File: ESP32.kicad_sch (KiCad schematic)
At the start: 6 parts, among them J9 PROG, U4 ESP32-WROOM-32D

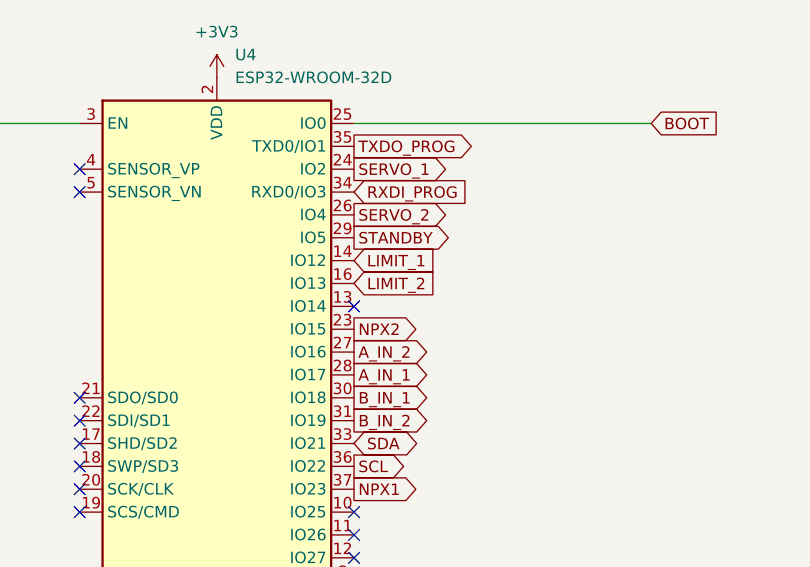
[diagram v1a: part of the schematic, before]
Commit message: Moved LIMIT1 signal away from IO12 where the pullup was stopping the ESP from booting
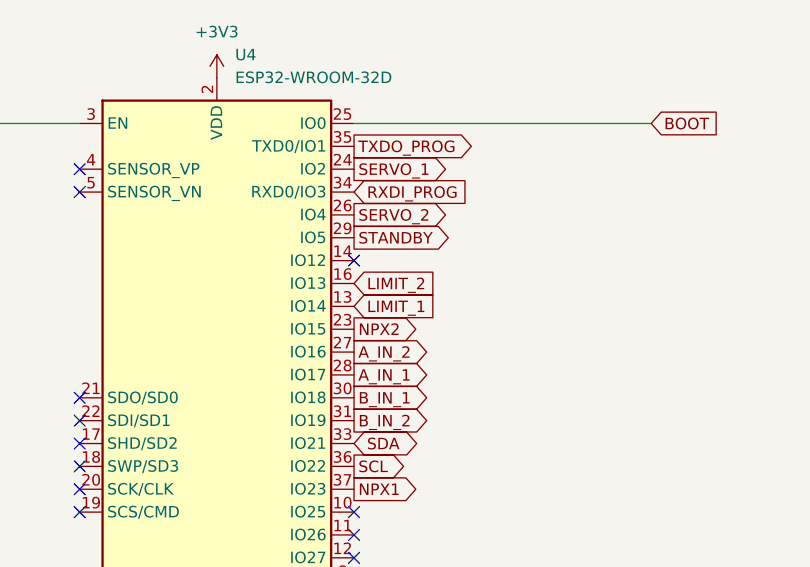
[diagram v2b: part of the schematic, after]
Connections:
- net LIMIT_1: now also U4.13 (IO14); no longer U4.14 (IO12)
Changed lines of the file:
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@@
   )
   (no_connect (at 223.52 106.68))
+  (no_connect (at 223.52 78.74))
   (no_connect (at 223.52 109.22))
   (no_connect (at 193.04 104.14))
@@
   (no_connect (at 193.04 68.58))
   (no_connect (at 193.04 71.12))
-  (no_connect (at 223.52 83.82))
   (no_connect (at 223.52 111.76))
   (polyline (pts (xy 124.46 24.13) (xy 124.46 161.29))
@@
     )
   )
-  (global_label "LIMIT_1" (shape input) (at 223.52 78.74 0) (fields_autoplaced)
-    (effects (font (size 1.27 1.27)) (justify left))
-    (property "Intersheet References" "${INTERSHEET_REFS}" (id 0) (at 232.7669 78.6606 0)
+  (global_label "LIMIT_1" (shape input) (at 223.52 83.82 0) (fields_autoplaced)
+    (effects (font (size 1.27 1.27)) (justify left))
+    (property "Intersheet References" "${INTERSHEET_REFS}" (id 0) (at 232.7669 83.7406 0)
       (effects (font (size 1.27 1.27)) (justify left) hide)
     )
@@
     (pin "6")
   )
-  (symbol (lib_name "+3V3_2") (lib_id "power:+3V3") (at 67.31 43.18 0) (unit 1)
+  (symbol (lib_id "power:+3V3") (at 67.31 43.18 0) (unit 1)
     (in_bom yes) (on_board yes) (fields_autoplaced)
     (property "Reference" "#PWR029" (id 0) (at 67.31 46.99 0)
@@
     (pin "1")
   )
-  (symbol (lib_name "+3V3_3") (lib_id "power:+3V3") (at 173.99 55.88 0) (unit 1)
+  (symbol (lib_id "power:+3V3") (at 173.99 55.88 0) (unit 1)
     (in_bom yes) (on_board yes) (fields_autoplaced)
     (property "Reference" "#PWR030" (id 0) (at 173.99 59.69 0)
@@
     (pin "9")
   )
-  (symbol (lib_name "GND_3") (lib_id "power:GND") (at 67.31 58.42 0) (unit 1)
+  (symbol (lib_id "power:GND") (at 67.31 58.42 0) (unit 1)
     (in_bom yes) (on_board yes) (fields_autoplaced)
     (property "Reference" "#PWR031" (id 0) (at 67.31 64.77 0)
@@
     (pin "1")
   )
-  (symbol (lib_name "GND_2") (lib_id "power:GND") (at 173.99 73.66 0) (unit 1)
+  (symbol (lib_id "power:GND") (at 173.99 73.66 0) (unit 1)
     (in_bom yes) (on_board yes) (fields_autoplaced)
     (property "Reference" "#PWR033" (id 0) (at 173.99 80.01 0)
@@
     (pin "2")
   )
-  (symbol (lib_name "+3V3_1") (lib_id "power:+3V3") (at 44.45 97.79 0) (unit 1)
+  (symbol (lib_id "power:+3V3") (at 44.45 97.79 0) (unit 1)
     (in_bom yes) (on_board yes) (fields_autoplaced)
     (property "Reference" "#PWR035" (id 0) (at 44.45 101.6 0)
@@
     (pin "1")
   )
-  (symbol (lib_name "GND_1") (lib_id "power:GND") (at 44.45 100.33 0) (unit 1)
+  (symbol (lib_id "power:GND") (at 44.45 100.33 0) (unit 1)
     (in_bom yes) (on_board yes) (fields_autoplaced)
     (property "Reference" "#PWR036" (id 0) (at 44.45 106.68 0)
